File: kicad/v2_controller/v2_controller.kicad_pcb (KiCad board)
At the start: 2 copper layers, 106 x 116 mm, 134 parts, among them J1 USB_C_Receptacle_USB2.0, J2 USB_C_Receptacle_USB2.0, J3 Conn_02x10_Odd_Even, J4 Conn_02x10_Odd_Even, J5 Conn_02x04_Odd_Even, J6 Conn_02x03_Odd_Even, Q1 S8050, Q2 S8050, SW18 Boot, SW19 Reset, U1 ESP32-S3-WROOM-1-N16R8, U2 SSD1306_I2C, U3 74AHCT1G125, U4 NCP167BMX330TBG, U5 USBLC6-2P6, U6 USBLC6-2P6, U7 CP2102N-Axx-xQFN24

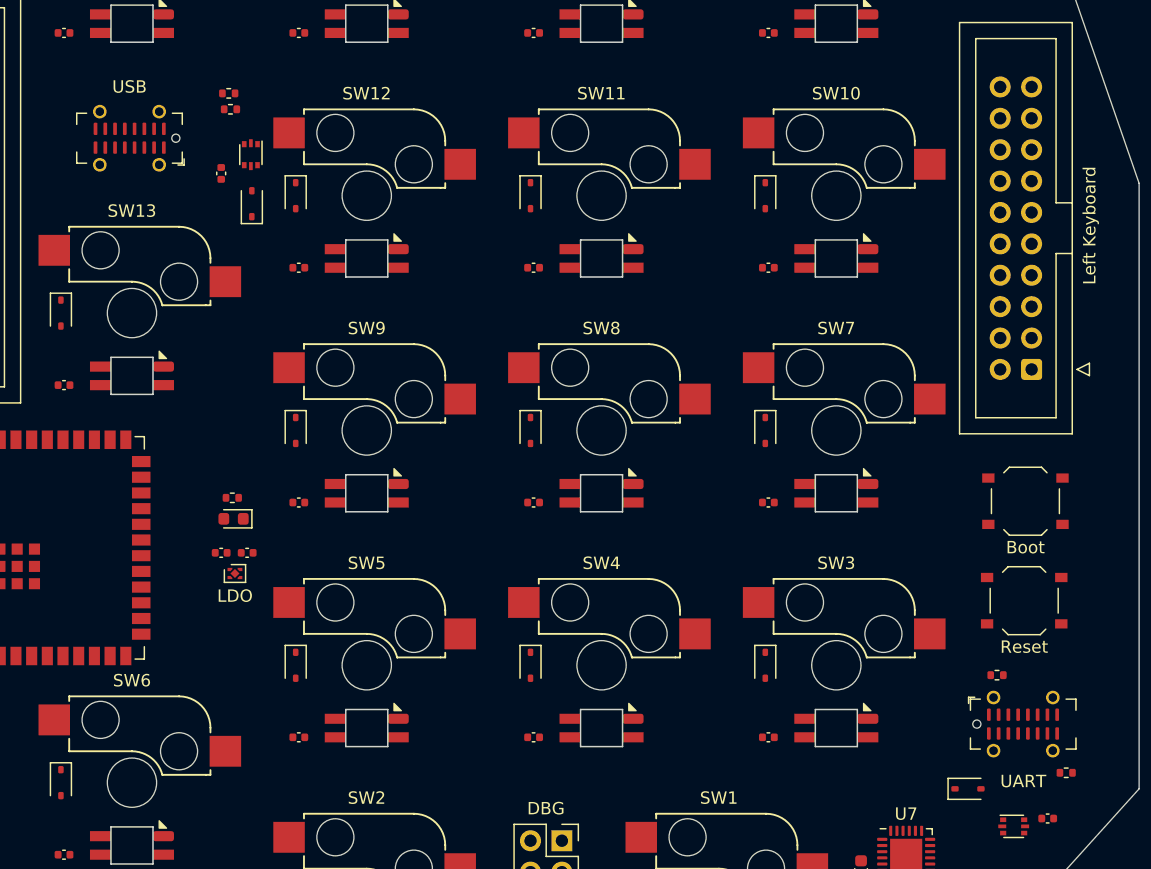
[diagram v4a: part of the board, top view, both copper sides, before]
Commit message: [kicad] switch USB receptacles again, and other PCB improvements
Switch the USB receptacles to GT-USB-7090B, since the GT-USB-7051A had
very limited space for routing traces.

Also add labels on the key switches, and check in 3d models for more
components.
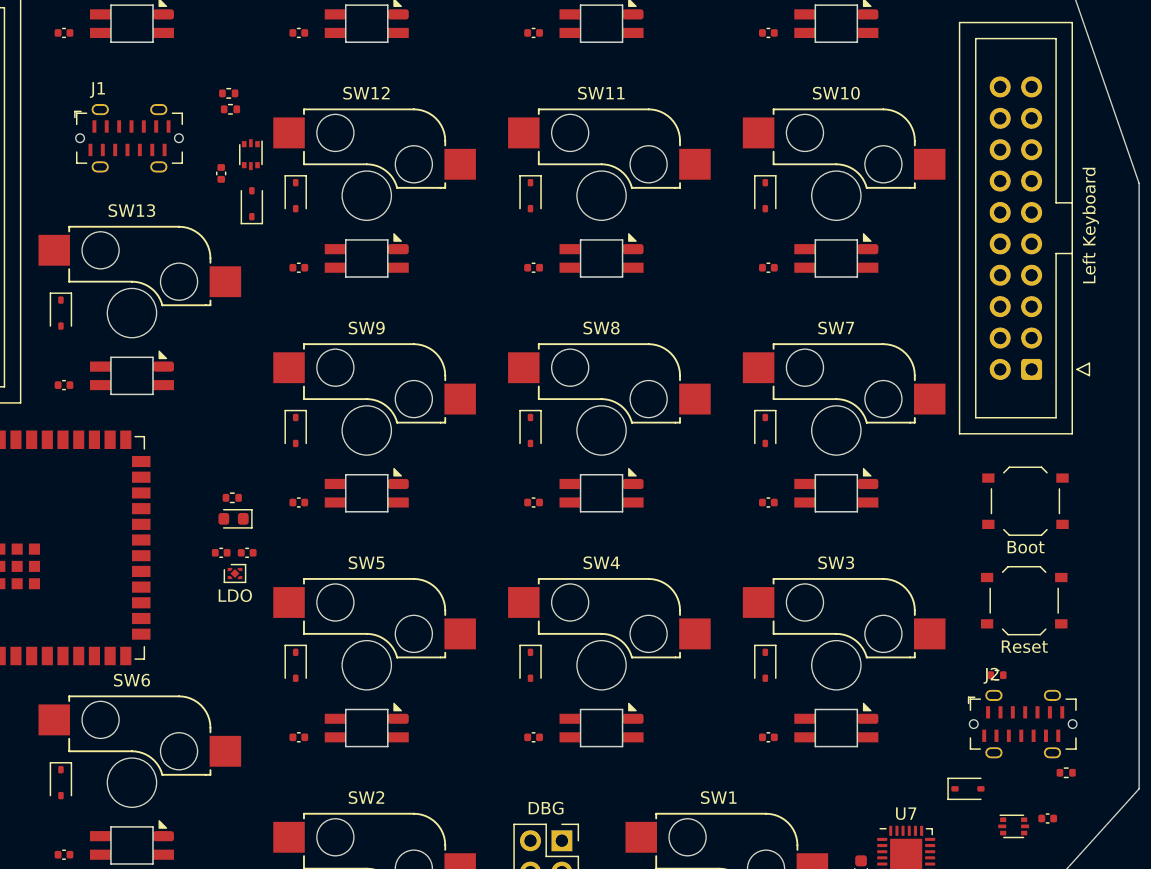
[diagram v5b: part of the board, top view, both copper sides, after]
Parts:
- J1, J2: footprint Connector_USB:USB_C_Receptacle_G-Switch_GT-USB-7051x -> mantyl:GT-USB-7090x
- SW1: value ~ -> KP0
- SW10: value ~ -> KP7
- SW11: value ~ -> KP8
- SW12: value ~ -> KP9
- SW13: value ~ -> KP_Plus
- SW14: value ~ -> KP_Extra
- SW15: value ~ -> KP_Divide
- SW16: value ~ -> KP_Multiply
- SW17: value ~ -> KP_Subtract
- SW2: value ~ -> KP_Dot
- SW3: value ~ -> KP1
- SW4: value ~ -> KP2
- SW5: value ~ -> KP3
- SW6: value ~ -> KP_Enter
- SW7: value ~ -> KP4
- SW8: value ~ -> KP5
- SW9: value ~ -> KP6
- turned J1 to 0 degrees
- renumbered REF** to MH1, REF** to MH2, REF** to MH3, REF** to MH4

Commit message: [kicad] begin routing some traces
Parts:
- U5: value USBLC6-2P6 -> USBLC6-2SC6; footprint Package_TO_SOT_SMD:SOT-666 -> Package_TO_SOT_SMD:SOT-23-6
- moved R9 39.0 mm to (72.2, 97.6), turned to 0 degrees
- moved U5 35.7 mm to (68.3, 99.3)
- moved D20 34.9 mm to (72.9, 127.9)
- moved R12 34.9 mm to (72.8, 126.2)
- moved D18 34.1 mm to (71.1, 101.8)
- moved U3 34.0 mm to (61.0, 132.0)
- moved C10 34.0 mm to (63.2, 132.7)
- moved C15 33.8 mm to (70.6, 98.9)
- moved J1 32.2 mm to (68.4, 93.8)
- moved R8 30.1 mm to (65.7, 89.9)
- moved C12 28.4 mm to (66.8, 124.2), turned to -90 degrees
- moved C11 28.3 mm to (70.0, 124.2), turned to -90 degrees
- moved U4 26.7 mm to (68.4, 124.2)
- moved R10 15.2 mm to (129.1, 120.8), turned to -90 degrees
- moved R14 13.4 mm to (128.5, 111.0), turned to 90 degrees
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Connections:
- U1 pad 10: unconnected-(U1-GPIO17/U1TXD-Pad10) -> /ESP32/COL8
- U1 pad 11: unconnected-(U1-GPIO18/U1RXD-Pad11) -> /ESP32/UART_RX
- U1 pad 12: unconnected-(U1-GPIO8-Pad12) -> /ESP32/UART_TX
- U1 pad 15: /ESP32/COL0 -> /ESP32/ROW0
- U1 pad 16: /ESP32/COL1 -> /ESP32/ROW1
- U1 pad 17: /ESP32/COL2 -> /ESP32/ROW2
- U1 pad 18: /ESP32/COL3 -> /ESP32/ROW3
- U1 pad 19: /ESP32/COL4 -> /ESP32/ROW4
- U1 pad 20: /ESP32/COL5 -> /ESP32/ROW5
- U1 pad 21: /ESP32/COL6 -> /ESP32/COL0
- U1 pad 22: /ESP32/COL7 -> /ESP32/COL1
- U1 pad 23: /ESP32/COL8 -> /ESP32/COL2
- U1 pad 24: /ESP32/COL9 -> /ESP32/COL3
- U1 pad 25: /ESP32/COL10 -> /ESP32/COL4
- U1 pad 26: unconnected-(U1-GPIO45-Pad26) -> /ESP32/COL5
- U1 pad 28: /ESP32/OLED_RST -> /ESP32/COL6
- U1 pad 29: /ESP32/LED_DIN_3V3 -> /ESP32/COL7
- U1 pad 30: /ESP32/ROW11 -> unconnected-(U1-GPIO37-Pad30)
- U1 pad 31: /ESP32/ROW10 -> unconnected-(U1-GPIO38-Pad31)
- U1 pad 32: /ESP32/ROW9 -> unconnected-(U1-GPIO39-Pad32)
- U1 pad 33: /ESP32/ROW8 -> unconnected-(U1-GPIO40-Pad33)
- U1 pad 34: /ESP32/ROW7 -> /ESP32/ROW11
- U1 pad 35: /ESP32/ROW6 -> /ESP32/ROW10
- U1 pad 36: /ESP32/UART_RX -> /ESP32/ROW9
- U1 pad 37: /ESP32/UART_TX -> /ESP32/ROW8
- U1 pad 38: /ESP32/SDA -> /ESP32/ROW7
- U1 pad 39: /ESP32/SCL -> /ESP32/ROW6
- U1 pad 4: /ESP32/ROW0 -> /ESP32/LED_DIN_3V3
- U1 pad 5: /ESP32/ROW1 -> /ESP32/OLED_RST
- U1 pad 6: /ESP32/ROW2 -> /ESP32/SCL
- U1 pad 7: /ESP32/ROW3 -> /ESP32/SDA
- U1 pad 8: /ESP32/ROW4 -> /ESP32/COL10
- U1 pad 9: /ESP32/ROW5 -> /ESP32/COL9
- U6 pad 1: Net-(J2-D--PadA7) -> Net-(J2-D+-PadA6)
- U6 pad 3: Net-(J2-D+-PadA6) -> Net-(J2-D--PadA7)
- U6 pad 4: /USB/UART_USB_D+ -> /USB/UART_USB_D-
- U6 pad 6: /USB/UART_USB_D- -> /USB/UART_USB_D+
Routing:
- net +3.3V: track 0.00 -> 179.6 mm, vias 0 -> 2
- net /ESP32/GPIO0: track 0.00 -> 137.7 mm, vias 0 -> 2
- net GND: track 0.00 -> 110.2 mm, vias 0 -> 15
- net /ESP32/UART_RX: track 0.00 -> 80.1 mm, vias 0 -> 2
- net Net-(D13-DOUT): track 0.00 -> 77.7 mm
- net Net-(D6-DOUT): track 0.00 -> 76.7 mm
- net /ESP32/UART_TX: track 0.00 -> 74.0 mm, vias 0 -> 2
- net /ESP32/ROW6: track 0.00 -> 73.2 mm
- net /ESP32/ROW7: track 0.00 -> 70.2 mm
- net Net-(D10-DIN): track 0.00 -> 67.1 mm, vias 0 -> 2
- net Net-(D2-DOUT): track 0.00 -> 59.4 mm, vias 0 -> 2
- net /ESP32/OLED_RST: track 0.00 -> 55.6 mm
- net /ESP32/SCL: track 0.00 -> 51.8 mm
- net /ESP32/SDA: track 0.00 -> 50.5 mm
- net /ESP32/ROW4: track 0.00 -> 42.1 mm
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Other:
- board size 106 x 116 mm -> 100 x 116 mm
- copper layers 2 -> 4

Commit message: [kicad] a little more trace routing
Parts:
- moved R12 2.42 mm to (70.8, 127.5), turned to 180 degrees
- moved D20 2.01 mm to (71.3, 129.1)
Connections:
- J6 pad 2: /ESP32/ROW0 -> /ESP32/ROW4
- J6 pad 3: /ESP32/ROW1 -> /ESP32/ROW5
- J6 pad 4: /ESP32/ROW2 -> /ESP32/ROW6
- J6 pad 5: /ESP32/ROW3 -> /ESP32/ROW7
- J6 pad 6: /ESP32/ROW4 -> /ESP32/ROW8
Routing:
- net /ESP32/ROW1: track 0.00 -> 44.9 mm
- net /ESP32/ROW2: track 0.00 -> 42.5 mm
- net /ESP32/ROW0: track 0.00 -> 42.1 mm
- net /ESP32/ROW3: track 0.00 -> 41.9 mm
- net /ESP32/SCL: track 51.8 -> 83.7 mm, vias 0 -> 2
- net /ESP32/ROW8: track 25.9 -> 55.8 mm, vias 0 -> 2
- net /ESP32/SDA: track 50.5 -> 79.6 mm, vias 0 -> 4
- net /ESP32/UART_TX: track 74.0 -> 87.2 mm, vias 2 -> 4
- net +3.3V: track 179.6 -> 189.9 mm, vias 2 -> 6
- net /ESP32/UART_RX: track 80.1 -> 89.0 mm
- net GND: track 110.2 -> 115.2 mm, vias 15 -> 17
- net Net-(D36-K): track 0.00 -> 4.25 mm
- net Net-(D35-K): track 0.00 -> 4.25 mm
- net Net-(D34-K): track 0.00 -> 4.25 mm
- net Net-(D32-K): track 0.00 -> 4.25 mm
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
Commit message: [kicad] more routing
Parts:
- moved C19 0.75 mm to (113.8, 53.8)
- moved C20 0.75 mm to (113.8, 72.8)
- moved C21 0.75 mm to (113.8, 91.8)
- moved C22 0.75 mm to (113.8, 110.8)
- moved C23 0.75 mm to (104.2, 129.8)
- moved C24 0.75 mm to (94.8, 53.8)
- moved C25 0.75 mm to (94.8, 72.8)
- moved C26 0.75 mm to (94.8, 91.8)
- moved C27 0.75 mm to (94.8, 110.8)
- moved C28 0.75 mm to (75.8, 53.8)
- moved C29 0.75 mm to (75.8, 72.8)
- moved C30 0.75 mm to (75.8, 91.8)
- moved C31 0.75 mm to (75.8, 110.8)
- moved C32 0.75 mm to (75.8, 129.8)
- moved C33 0.75 mm to (56.8, 53.8)
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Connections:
- D17 pad 2: /ESP32/LED_LEFT_DIN -> /ESP32/LED_RIGHT_DIN
- J3 pad 10: /ESP32/COL3 -> /ESP32/COL4
- J3 pad 11: /ESP32/ROW4 -> /ESP32/ROW1
- J3 pad 12: /ESP32/COL4 -> /ESP32/COL3
- J3 pad 13: /ESP32/ROW5 -> /ESP32/ROW0
- J3 pad 14: /ESP32/COL5 -> /ESP32/COL2
- J3 pad 16: /ESP32/COL6 -> /ESP32/COL1
- J3 pad 17: /ESP32/LED_RIGHT_DIN -> unconnected-(J3-Pin_17-Pad17)
- J3 pad 18: /ESP32/COL7 -> /ESP32/COL0
- J3 pad 3: /ESP32/ROW0 -> /ESP32/ROW5
- J3 pad 4: /ESP32/COL0 -> /ESP32/COL7
- J3 pad 5: /ESP32/ROW1 -> /ESP32/ROW4
- J3 pad 6: /ESP32/COL1 -> /ESP32/COL6
- J3 pad 7: /ESP32/ROW2 -> /ESP32/ROW3
- J3 pad 8: /ESP32/COL2 -> /ESP32/COL5
- J3 pad 9: /ESP32/ROW3 -> /ESP32/ROW2
- J4 pad 17: unconnected-(J4-Pin_17-Pad17) -> /ESP32/LED_LEFT_DIN
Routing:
- net /ESP32/COL8: track 0.00 -> 179.5 mm, vias 0 -> 6
- net /ESP32/COL9: track 0.00 -> 169.0 mm, vias 0 -> 4
- net /ESP32/COL0: track 0.00 -> 142.4 mm
- net /ESP32/CHIP_PU: track 16.0 -> 149.7 mm, vias 2 -> 4
- net /ESP32/COL1: track 0.00 -> 128.5 mm, vias 0 -> 3
- net /ESP32/COL5: track 0.00 -> 127.9 mm, vias 0 -> 4
- net /ESP32/COL2: track 0.00 -> 127.7 mm, vias 0 -> 4
- net /ESP32/COL4: track 0.00 -> 127.5 mm, vias 0 -> 4
- net /ESP32/COL3: track 0.00 -> 127.2 mm, vias 0 -> 4
- net /ESP32/COL6: track 0.00 -> 122.5 mm, vias 0 -> 2
- net /ESP32/COL7: track 0.00 -> 122.5 mm, vias 0 -> 2
- net /ESP32/ROW1: track 44.9 -> 161.0 mm, vias 0 -> 2
- net /ESP32/ROW0: track 42.1 -> 153.1 mm, vias 0 -> 2
- net /ESP32/LED_LEFT_DIN: track 0.00 -> 97.4 mm, vias 0 -> 1
- net /ESP32/ROW5: track 0.00 -> 92.2 mm, vias 0 -> 2
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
